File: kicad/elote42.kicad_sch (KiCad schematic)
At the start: 86 parts, among them SW1 SW_Push, U1 ProMicro

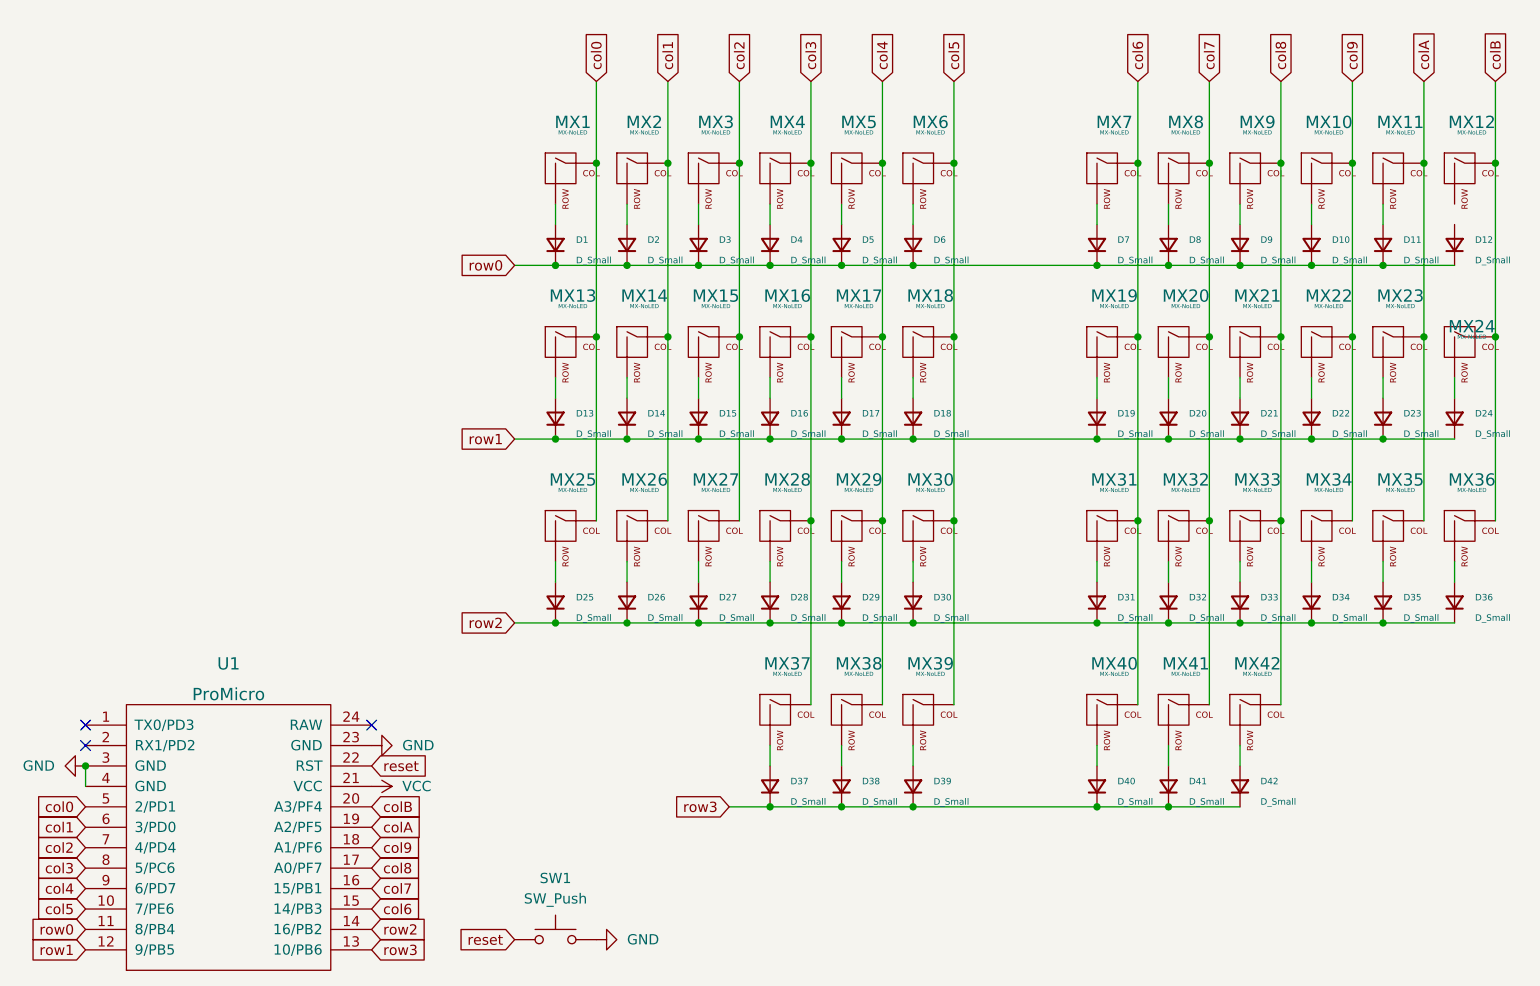
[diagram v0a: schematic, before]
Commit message: Routed diodes to corresponding switches
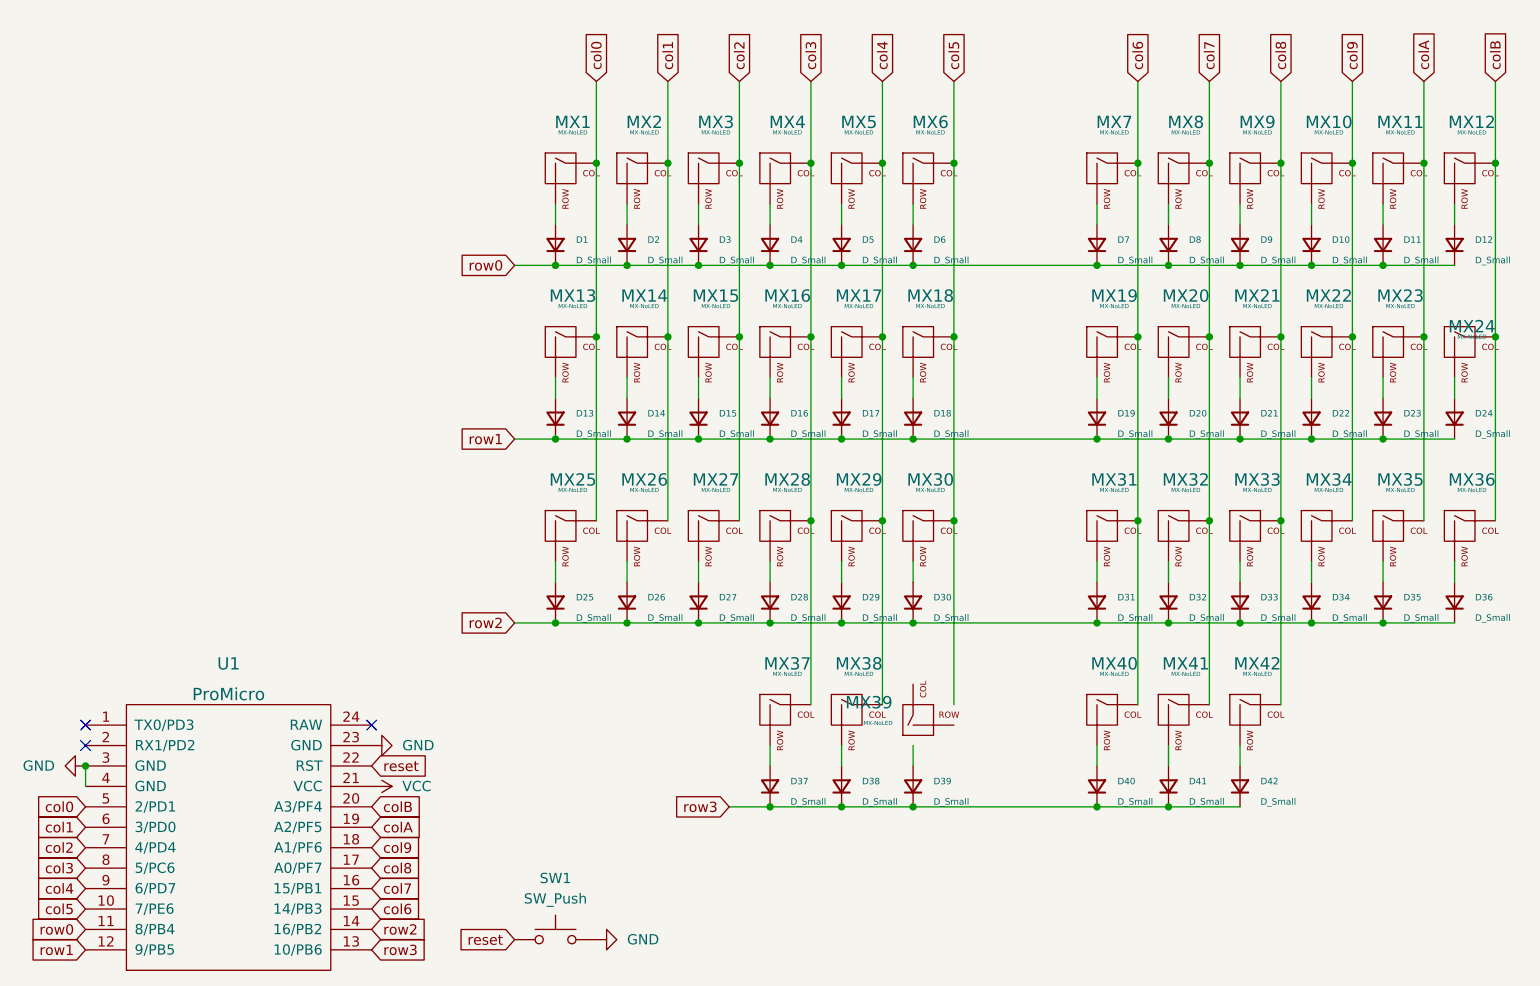
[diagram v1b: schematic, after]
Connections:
- net col5: no longer MX39.1 (COL)
- net at D39.2 (A): no longer MX39.2 (ROW)
- net at MX12.2 (ROW): now also D12.2 (A)
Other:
- moved on the sheet: MX39
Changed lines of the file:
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@@
+    (stroke (width 0) (type default) (color 0 0 0 0))
+  )
+  (wire (pts (xy 204.47 52.07) (xy 204.47 54.61))
     (stroke (width 0) (type default) (color 0 0 0 0))
   )
@@
     (pin "2")
   )
-  (symbol (lib_id "MX_Alps_Hybrid:MX-NoLED") (at 138.43 115.57 0) (unit 1)
-    (in_bom yes) (on_board yes) (fields_autoplaced)
-    (property "Reference" "MX39" (id 0) (at 139.3156 109.22 0)
-      (effects (font (size 1.524 1.524)))
-    )
-    (property "Value" "MX-NoLED" (id 1) (at 139.3156 110.49 0)
-      (effects (font (size 0.508 0.508)))
-    )
-    (property "Footprint" "MX_Alps_Hybrid:MX-1U-NoLED" (id 2) (at 122.555 116.205 0)
-      (effects (font (size 1.524 1.524)) hide)
-    )
-    (property "Datasheet" "" (id 3) (at 122.555 116.205 0)
-      (effects (font (size 1.524 1.524)) hide)
-    )
+  (symbol (lib_id "MX_Alps_Hybrid:MX-NoLED") (at 138.43 115.57 90) (unit 1)
+    (in_bom yes) (on_board yes) (fields_autoplaced)
+    (property "Reference" "MX39" (id 0) (at 134.62 114.0494 90)
+      (effects (font (size 1.524 1.524)) (justify left))
+    )
+    (property "Value" "MX-NoLED" (id 1) (at 134.62 116.5893 90)
+      (effects (font (size 0.508 0.508)) (justify left))
+    )
+    (property "Footprint" "MX_Alps_Hybrid:MX-1U-NoLED" (id 2) (at 139.065 131.445 0)
+      (effects (font (size 1.524 1.524)) hide)
+    )
+    (property "Datasheet" "" (id 3) (at 139.065 131.445 0)
+      (effects (font (size 1.524 1.524)) hide)
+    )

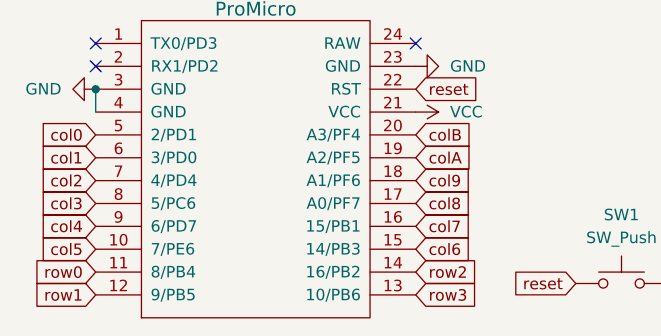
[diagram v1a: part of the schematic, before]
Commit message: row orientation swapped
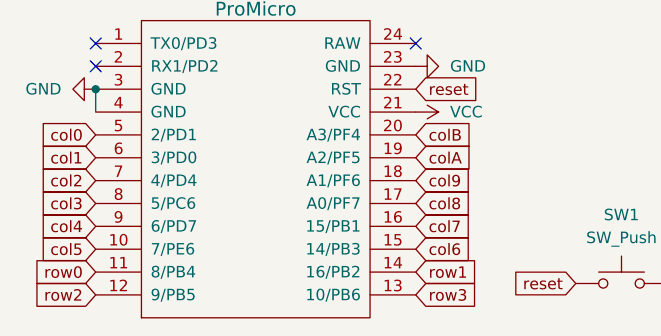
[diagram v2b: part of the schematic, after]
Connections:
- net row1: now also U1.14 (16/PB2); no longer U1.12 (9/PB5)
- net row2: now also U1.12 (9/PB5); no longer U1.14 (16/PB2)
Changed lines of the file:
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@@
     )
   )
-  (global_label "row2" (shape input) (at 69.85 142.24 0) (fields_autoplaced)
+  (global_label "row1" (shape input) (at 69.85 142.24 0) (fields_autoplaced)
     (effects (font (size 1.27 1.27)) (justify left))
     (property "Intersheet References" "${INTERSHEET_REFS}" (id 0) (at 76.7383 142.1606 0)
@@
     )
   )
-  (global_label "row1" (shape input) (at 34.29 144.78 180) (fields_autoplaced)
+  (global_label "row2" (shape input) (at 34.29 144.78 180) (fields_autoplaced)
     (effects (font (size 1.27 1.27)) (justify right))
     (property "Intersheet References" "${INTERSHEET_REFS}" (id 0) (at 27.4017 144.7006 0)
